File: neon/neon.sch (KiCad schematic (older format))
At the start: 41 parts, among them J1 V3V3-VIO, J2 V3V3-GND, J3 V3V3-GND, J4 V3V3-GND, J5 VBUS-VCC, Q1 BC807, Q2 BC807, Q3 BC807, Q4 BC807, Q5 BC807, Q6 BC807, Q7 BC807, Q8 BC807, U2 ABUS, U3 BBUS, U4 CBUS, U5 DBUS

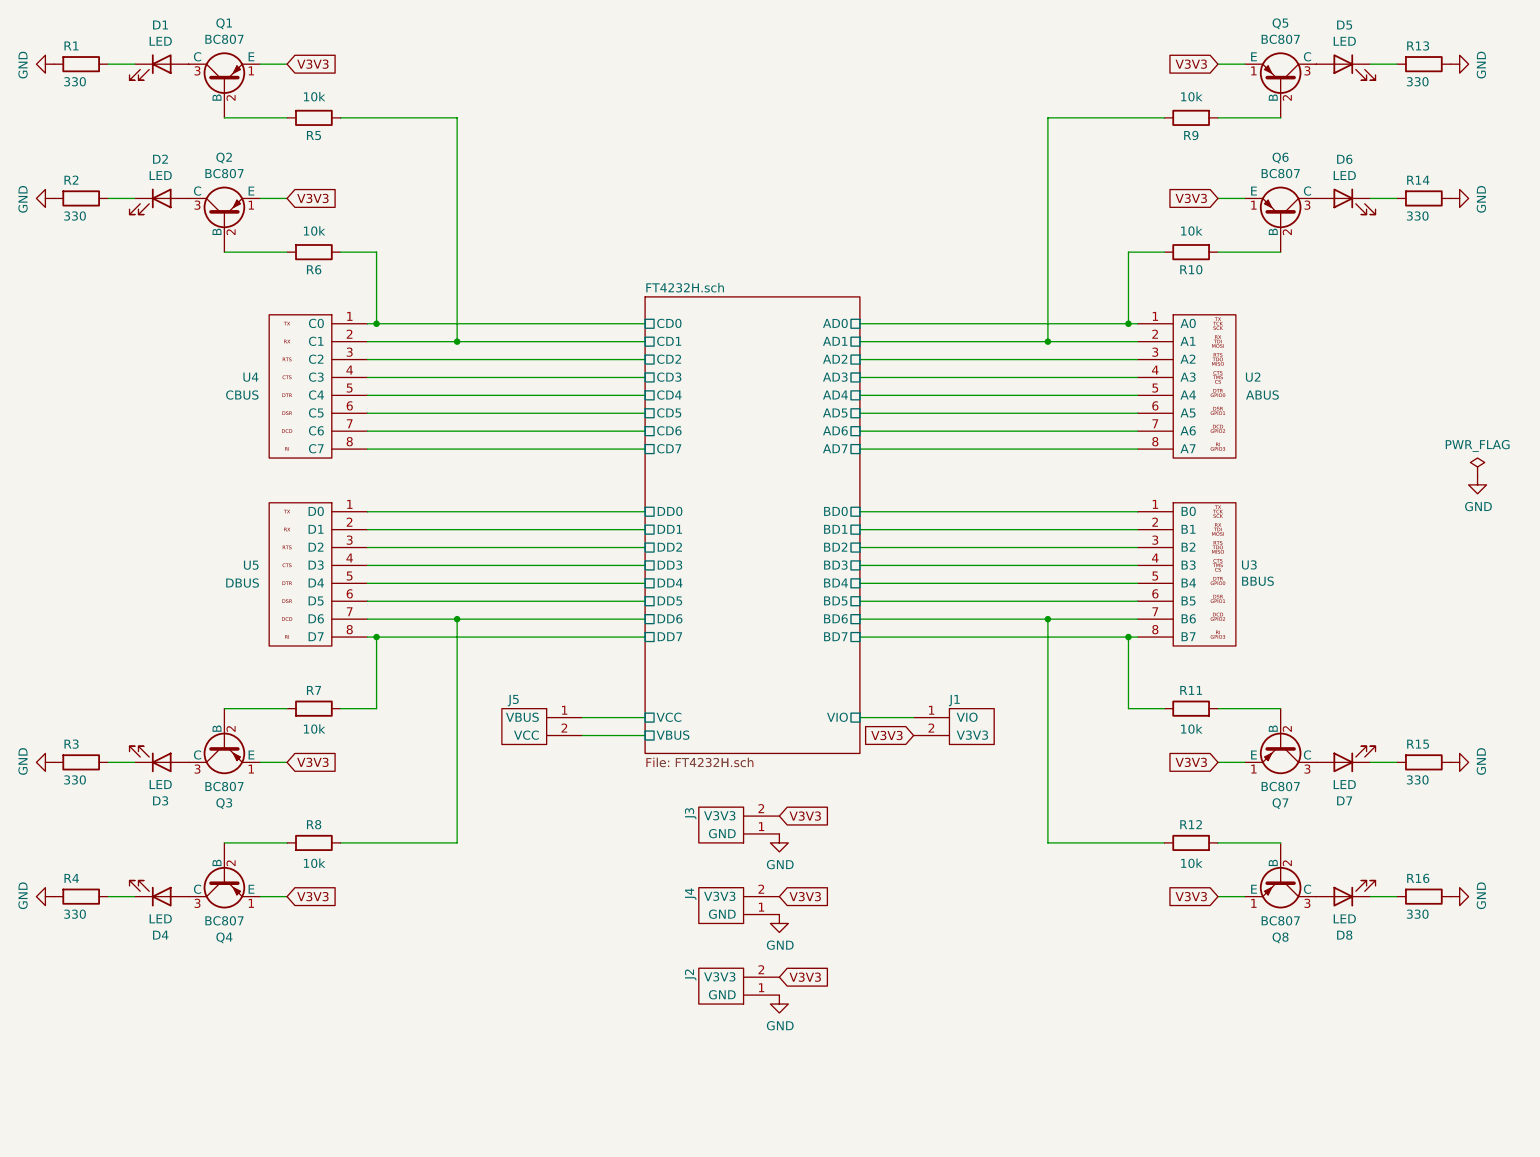
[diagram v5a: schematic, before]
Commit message: Version with shift register - schematic
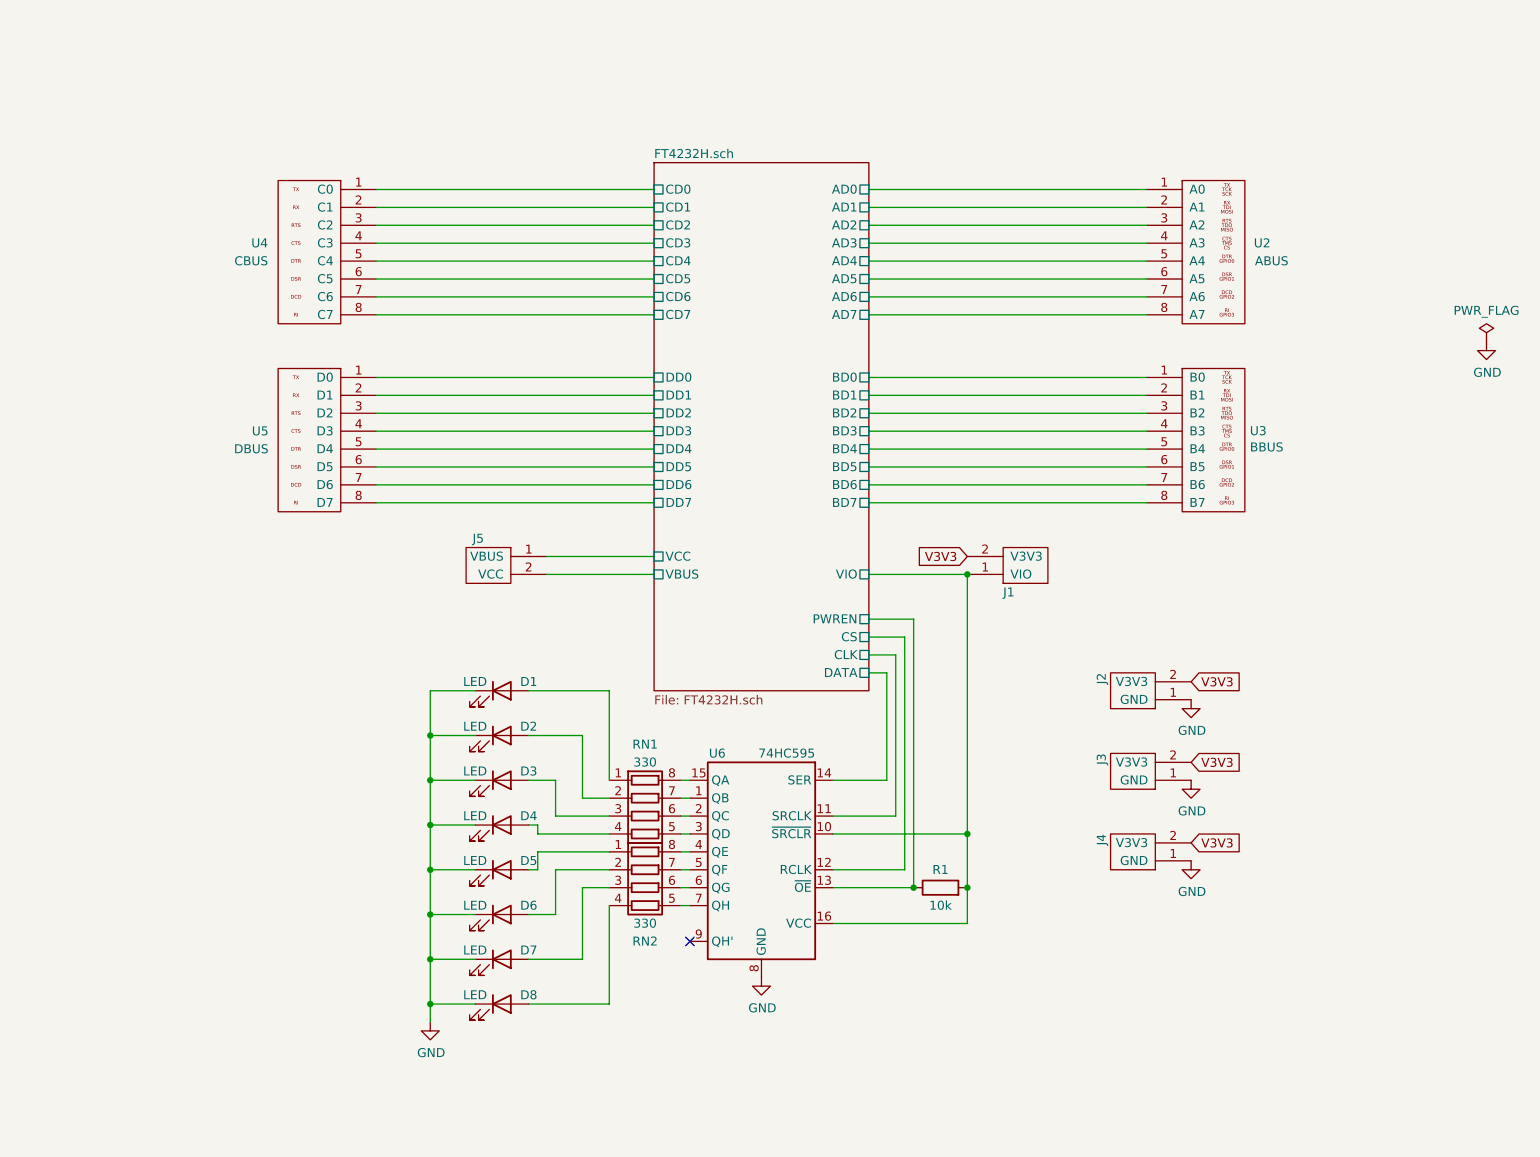
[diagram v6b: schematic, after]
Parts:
- removed Q1, Q2, Q3, Q4, Q5, Q6, Q7, Q8: BC807, Package_TO_SOT_SMD:SOT-23, symbol FTDI_transistors:BC807
- removed R10, R11, R12, R5, R6, R7, R8, R9: 10k, Resistor_SMD:R_0805_2012Metric, symbol Device:R
- removed R13, R14, R15, R16, R2, R3, R4: 330, Resistor_SMD:R_0805_2012Metric, symbol Device:R
- added RN1, RN2: 330, Resistor_SMD:R_Array_Convex_4x0603, symbol FTDI:R_Pack04
- added U6: 74HC595, Package_SO:SOIC-16_3.9x9.9mm_P1.27mm, symbol FTDI:74HC595
- R1: value 330 -> 10k
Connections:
- net FT4232H.sch/VIO: now also R1.2, U6.10 (~SRCLR), U6.16 (VCC)
- net GND: now also D1.1 (K), D2.1 (K), D3.1 (K), D4.1 (K), D5.1 (K), D6.1 (K), D7.1 (K), D8.1 (K), U6.8 (GND); no longer R1.2
- net at D1.2 (A): now also RN1.1 (R1.1)
- net FT4232H.sch/PWREN: now reaches R1.1
- net FT4232H.sch/PWREN: now also U6.13 (~OE); no longer D1.1 (K)
- net at D2.2 (A): now also RN1.2 (R2.1)
- net at D5.2 (A): now also RN2.1 (R1.1)
- net at D6.2 (A): now also RN2.2 (R2.1)
- net at D7.2 (A): now also RN2.3 (R3.1)
- net at D8.2 (A): now also RN2.4 (R4.1)
- net at D3.2 (A): now also RN1.3 (R3.1)
- net at D4.2 (A): now also RN1.4 (R4.1)
- new net: RN1.7 (R2.2), U6.1 (QB)
- new net: RN1.8 (R1.2), U6.15 (QA)
- new net: RN1.6 (R3.2), U6.2 (QC)
- new net: RN1.5 (R4.2), U6.3 (QD)
- new net: RN2.8 (R1.2), U6.4 (QE)
- new net: RN2.7 (R2.2), U6.5 (QF)
- new net: RN2.6 (R3.2), U6.6 (QG)
- new net: RN2.5 (R4.2), U6.7 (QH)
- new net FT4232H.sch/CLK: U6.11 (SRCLK)
- new net FT4232H.sch/CS: U6.12 (RCLK)
- new net FT4232H.sch/DATA: U6.14 (SER)
- no-connect marks 0 -> 1
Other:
- moved on the sheet: J1, J2, J3, J4, J5, U2, U3, U4, U5

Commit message: Texts ideas
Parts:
- U2, U3, U4, U5: footprint Connector_PinHeader_2.54mm:PinHeader_1x08_P2.54mm_Vertical -> neon_footprints:PinHeader_1x08_P2.54mm_Vertical
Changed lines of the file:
@@
 F 0 "U5" H 3900 3050 50  0000 C CNN
 F 1 "DBUS" H 3950 2950 50  0000 C CNN
-F 2 "Connector_PinHeader_2.54mm:PinHeader_1x08_P2.54mm_Vertical" H 3425 3725 50  0001 C CNN
+F 2 "neon_footprints:PinHeader_1x08_P2.54mm_Vertical" H 3425 3725 50  0001 C CNN
 F 3 "" H 3425 3725 50  0001 C CNN
 	1    3450 3050
@@
 F 0 "U4" H 3950 2000 50  0000 R CNN
 F 1 "CBUS" H 3950 1900 50  0000 C CNN
-F 2 "Connector_PinHeader_2.54mm:PinHeader_1x08_P2.54mm_Vertical" H 3425 2675 50  0001 C CNN
+F 2 "neon_footprints:PinHeader_1x08_P2.54mm_Vertical" H 3425 2675 50  0001 C CNN
 F 3 "" H 3425 2675 50  0001 C CNN
 	1    3450 2000
@@
 F 0 "U2" H 8550 2000 50  0000 L CNN
 F 1 "ABUS" H 8650 1900 50  0000 C CNN
-F 2 "Connector_PinHeader_2.54mm:PinHeader_1x08_P2.54mm_Vertical" H 8125 2675 50  0001 C CNN
+F 2 "neon_footprints:PinHeader_1x08_P2.54mm_Vertical" H 8125 2675 50  0001 C CNN
 F 3 "" H 8125 2675 50  0001 C CNN
 	1    8150 2000
@@
 F 0 "U3" H 8528 3051 50  0000 L CNN
 F 1 "BBUS" H 8528 2960 50  0000 L CNN
-F 2 "Connector_PinHeader_2.54mm:PinHeader_1x08_P2.54mm_Vertical" H 8125 3725 50  0001 C CNN
+F 2 "neon_footprints:PinHeader_1x08_P2.54mm_Vertical" H 8125 3725 50  0001 C CNN
 F 3 "" H 8125 3725 50  0001 C CNN
 	1    8150 3050

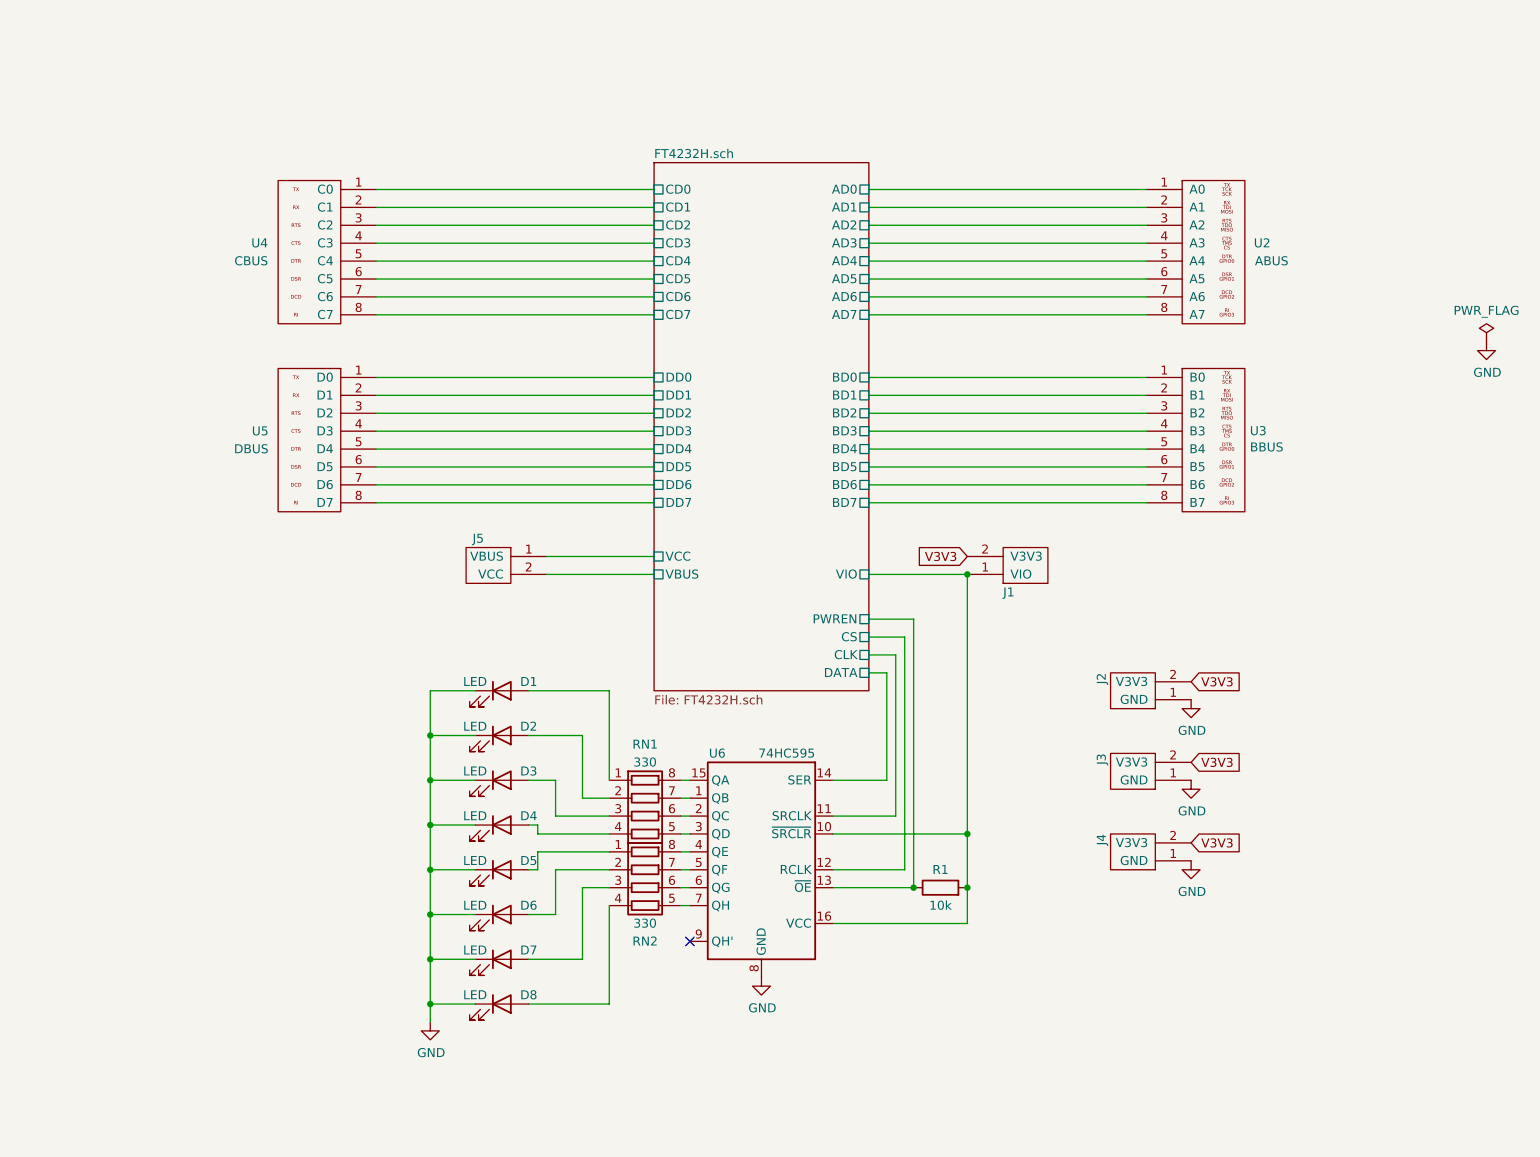
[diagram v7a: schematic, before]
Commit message: Add sniffer
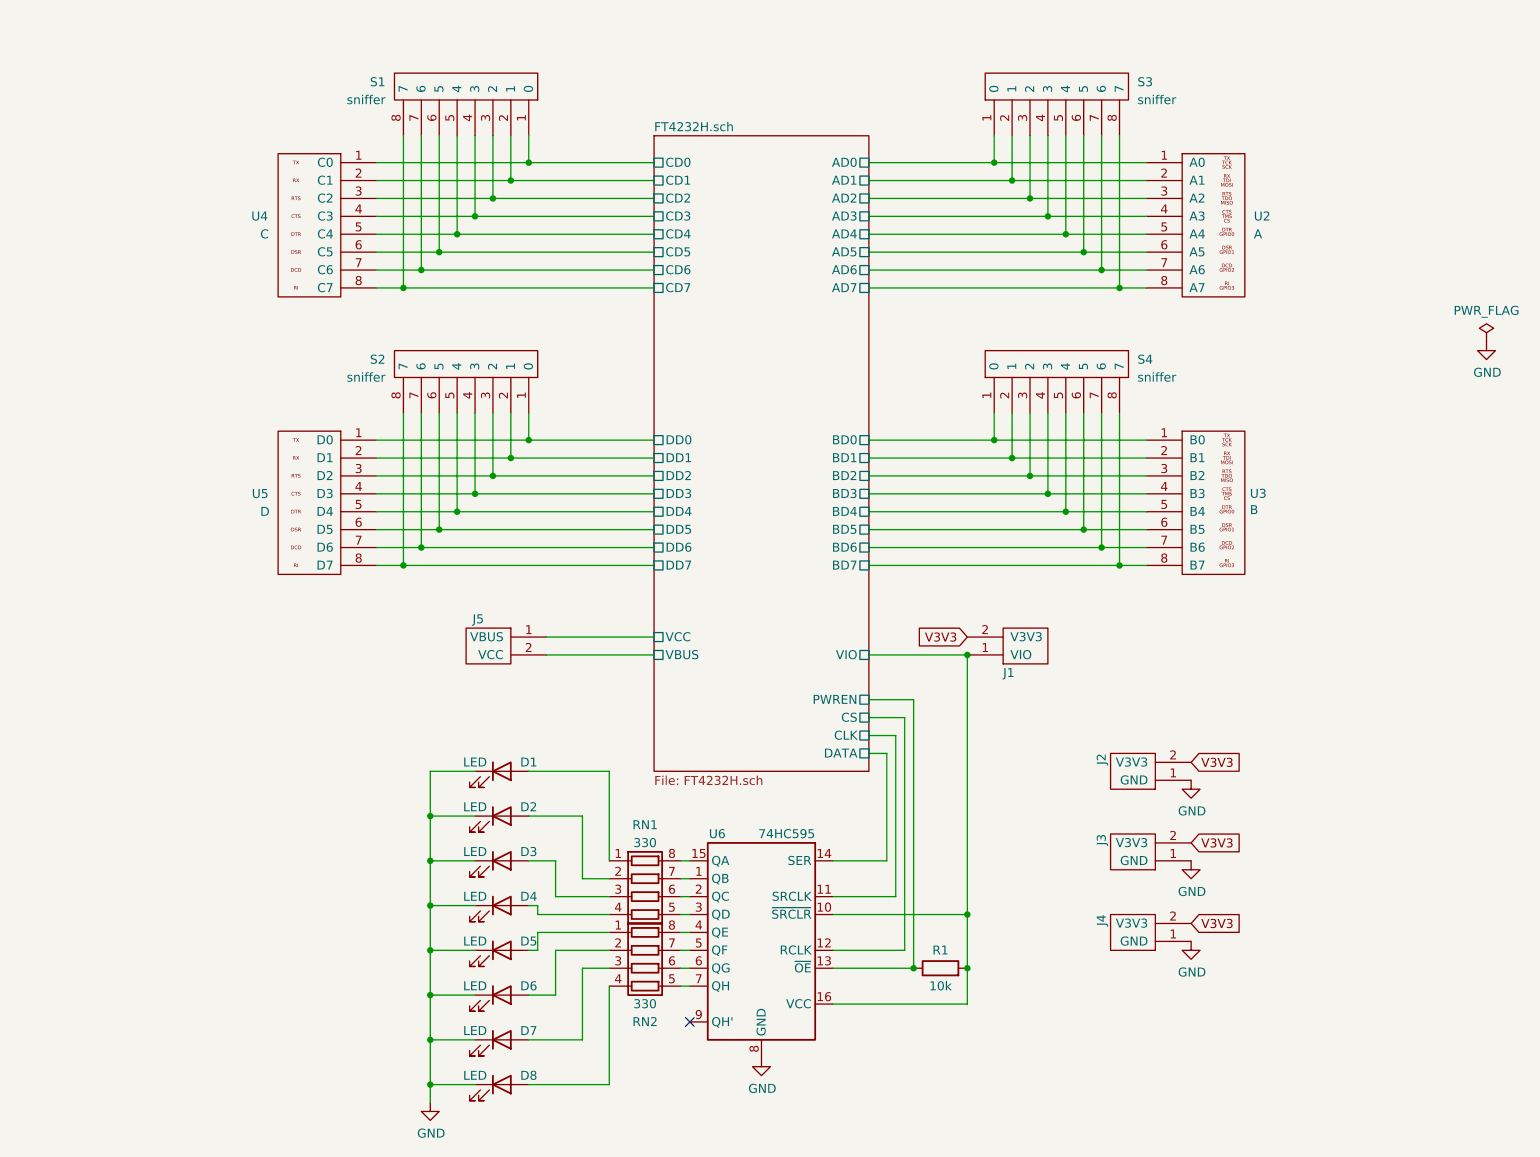
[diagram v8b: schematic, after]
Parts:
- added S1, S2, S3, S4: sniffer, neon_footprints:PinHeader_1x08_P2.54mm_Vertical, symbol FTDI:sniffer
- U2: value ABUS -> A
- U3: value BBUS -> B
- U4: value CBUS -> C
- U5: value DBUS -> D
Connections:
- net FT4232H.sch/AD0: now also S3.1 (0)
- net FT4232H.sch/AD1: now also S3.2 (1)
- net FT4232H.sch/AD2: now also S3.3 (2)
- net FT4232H.sch/AD3: now also S3.4 (3)
- net FT4232H.sch/AD4: now also S3.5 (4)
- net FT4232H.sch/AD5: now also S3.6 (5)
- net FT4232H.sch/AD6: now also S3.7 (6)
- net FT4232H.sch/AD7: now also S3.8 (7)
- net FT4232H.sch/BD0: now also S4.1 (0)
- net FT4232H.sch/BD1: now also S4.2 (1)
- net FT4232H.sch/BD2: now also S4.3 (2)
- net FT4232H.sch/BD3: now also S4.4 (3)
- net FT4232H.sch/BD4: now also S4.5 (4)
- net FT4232H.sch/BD5: now also S4.6 (5)
- net FT4232H.sch/BD6: now also S4.7 (6)
- net FT4232H.sch/BD7: now also S4.8 (7)
- net FT4232H.sch/CD0: now also S1.1 (0)
- net FT4232H.sch/CD1: now also S1.2 (1)
- net FT4232H.sch/CD2: now also S1.3 (2)
- net FT4232H.sch/CD3: now also S1.4 (3)
- net FT4232H.sch/CD4: now also S1.5 (4)
- net FT4232H.sch/CD5: now also S1.6 (5)
- net FT4232H.sch/CD6: now also S1.7 (6)
- net FT4232H.sch/CD7: now also S1.8 (7)
- net FT4232H.sch/DD0: now also S2.1 (0)
- net FT4232H.sch/DD1: now also S2.2 (1)
- net FT4232H.sch/DD2: now also S2.3 (2)
- net FT4232H.sch/DD3: now also S2.4 (3)
- net FT4232H.sch/DD4: now also S2.5 (4)
- net FT4232H.sch/DD5: now also S2.6 (5)
- net FT4232H.sch/DD6: now also S2.7 (6)
- net FT4232H.sch/DD7: now also S2.8 (7)
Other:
- moved on the sheet: D1, D2, D3, D4, D5, D6, D7, D8, J1, J2, J3, J4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
